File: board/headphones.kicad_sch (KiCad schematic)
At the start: 8 parts, among them J1701 HP

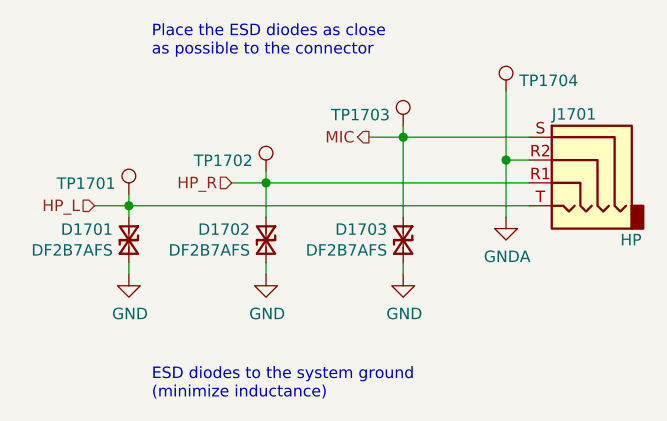
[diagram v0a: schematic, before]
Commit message: Added testpoints and other fixes
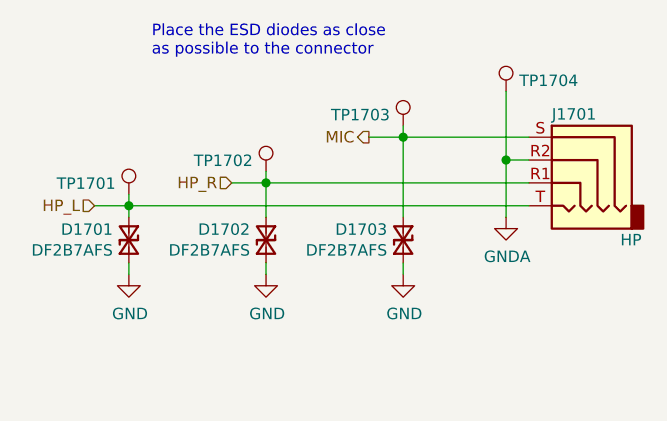
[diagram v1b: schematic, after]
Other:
- note removed: "ESD diodes to the system ground (minimize inductance)"
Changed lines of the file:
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@@
-    (effects (font (size 1.27 1.27)) (justify left bottom))
-  )
-  (text "ESD diodes to the system ground\n(minimize inductance)"
-    (at 137.16 118.11 0)
     (effects (font (size 1.27 1.27)) (justify left bottom))
   )
@@
       (effects (font (size 1.27 1.27)) hide)
     )
-    (property "Datasheet" "https://eu.mouser.com/datasheet/2/408/DF2B7AFS_datasheet_en_20180110-1128342.pdf" (id 3) (at 134.62 99.568 90)
+    (property "Datasheet" "~" (id 3) (at 134.62 99.568 90)
       (effects (font (size 1.27 1.27)) hide)
     )
@@
       (effects (font (size 1.27 1.27)) hide)
     )
-    (property "Datasheet" "https://eu.mouser.com/datasheet/2/408/DF2B7AFS_datasheet_en_20180110-1128342.pdf" (id 3) (at 149.86 99.568 90)
+    (property "Datasheet" "~" (id 3) (at 149.86 99.568 90)
       (effects (font (size 1.27 1.27)) hide)
     )
@@
       (effects (font (size 1.27 1.27)) hide)
     )
-    (property "Datasheet" "https://eu.mouser.com/datasheet/2/408/DF2B7AFS_datasheet_en_20180110-1128342.pdf" (id 3) (at 165.1 99.568 90)
-      (effects (font (size 1.27 1.27)) hide)
-    )
+    (property "Datasheet" "~" (id 3) (at 165.1 99.568 90)
+      (effects (font (size 1.27 1.27)) hide)
+    )
